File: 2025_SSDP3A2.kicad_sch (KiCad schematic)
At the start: 58 parts, among them J1 SolderPad, J2 SolderPad, J3 SolderPad, J4 SolderPad, J5 SolderPad_01x05, Q1 IAUZ30N10S5L240, Q2 BSZ096N10LS5, U1 LM5146RGYR

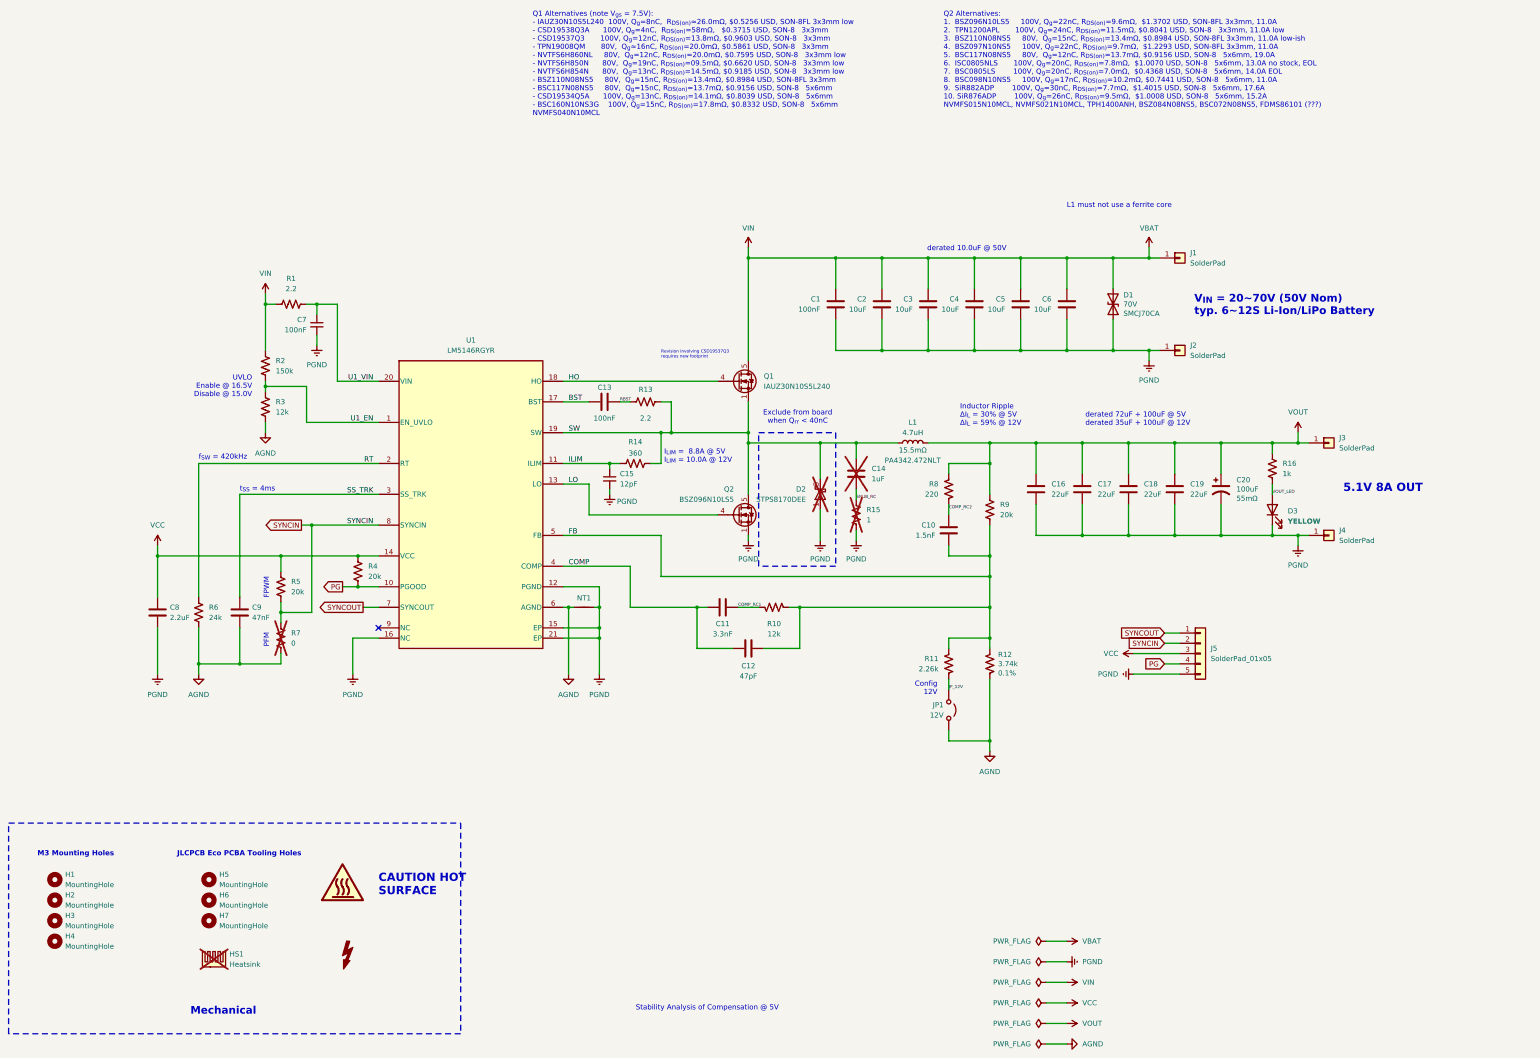
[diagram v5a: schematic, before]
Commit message: Added 7.4V output support
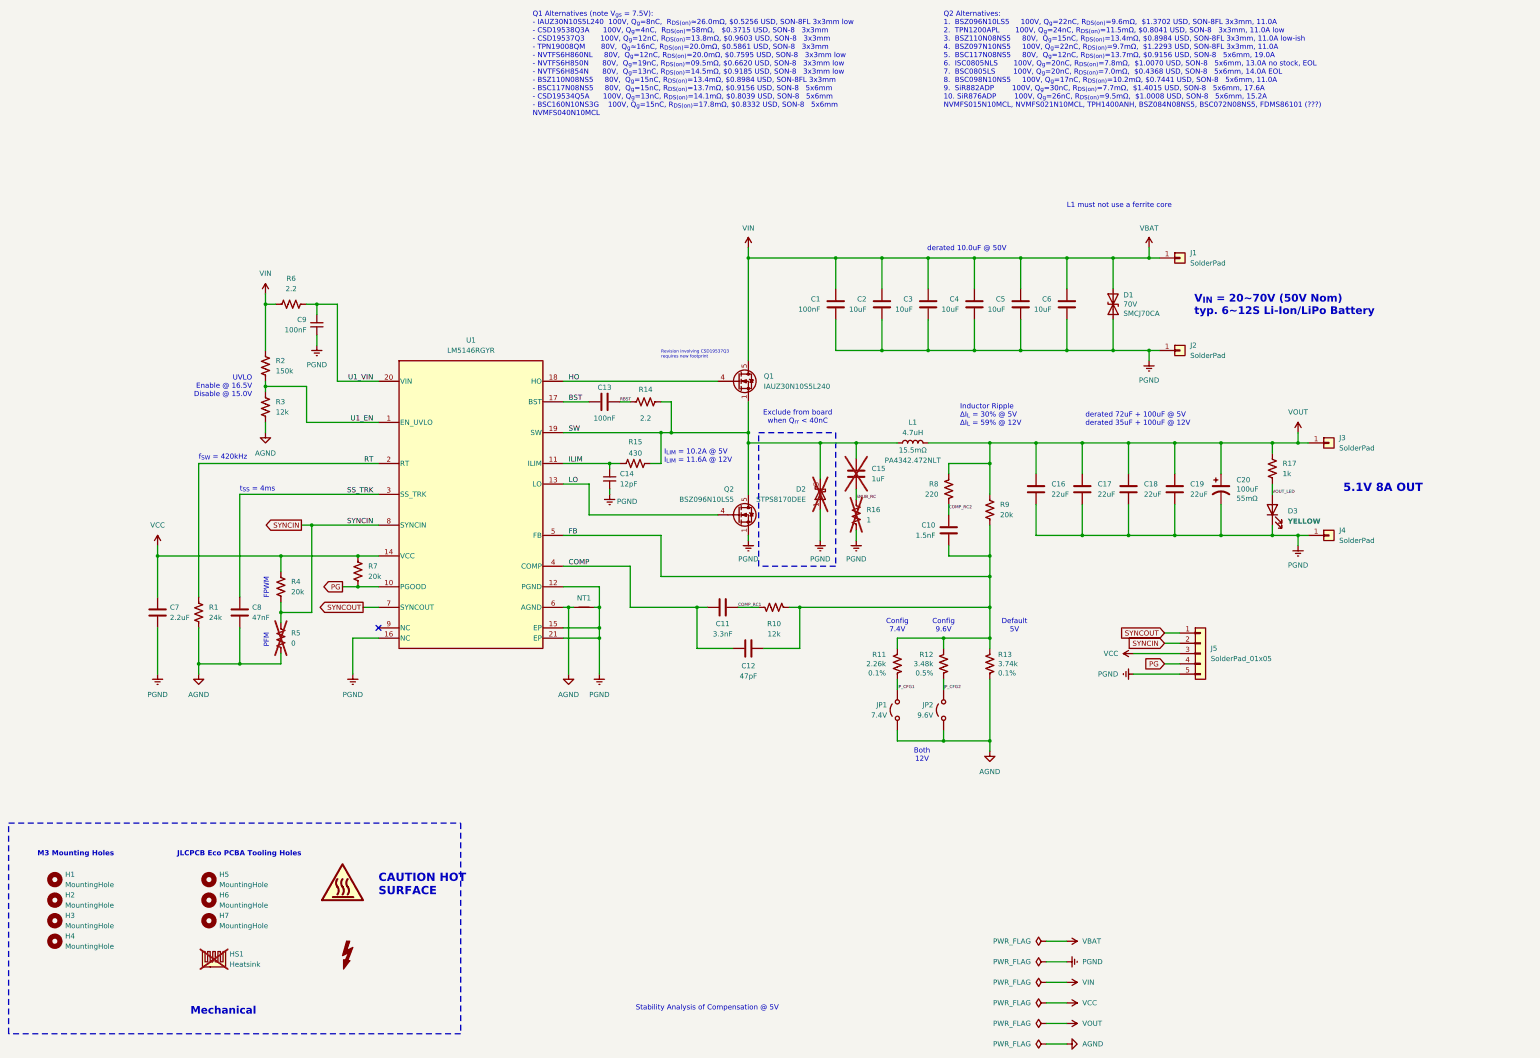
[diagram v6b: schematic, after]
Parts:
- added JP2: 9.6V, Jumper:SolderJumper-2_P1.3mm_Open_TrianglePad1.0x1.5mm, symbol Jumper:Jumper_2_Open
- added R12: 3.48k, Resistor_SMD:R_0603_1608Metric, symbol Device:R_US
- JP1: value 12V -> 7.4V
- R11: LCSC PN C667565 -> C861538; MANUFACTURER Guangdong Fenghua -> YAGEO; Tolerance 1% -> 0.1%
- R15: renamed from R14; value 360 -> 430; LCSC PN C25194 -> C23170
- renumbered C15 to C14, C14 to C15, C8 to C7, C9 to C8, C7 to C9, R6 to R1, R12 to R13, R13 to R14, R15 to R16, R16 to R17, R5 to R4, R7 to R5, R1 to R6, R4 to R7
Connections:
- net AGND: now also JP2.1 (A)
- net FB: now also R12.1
- net JP_12V renamed JP_CFG1
- new net JP_CFG2: JP2.2 (B), R12.2
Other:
- note added: "Both 12V"
- note added: "Config 7.4V"
- note added: "Config 9.6V"
- note added: "Default 5V"
- note added: "I_{LIM} = 10.2A @ 5V I_{LIM} = 11.6A @ 12V"
- note removed: "Config 12V"
- note removed: "I_{LIM} = 8.8A @ 5V I_{LIM} = 10.0A @ 12V"
- moved on the sheet: JP1, R11

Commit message: Final tweaks
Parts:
- HS1: value Heatsink -> 567-45AB
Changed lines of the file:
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@@
 			)
 		)
-		(property "Value" "Heatsink"
+		(property "Value" "567-45AB"
 			(at 77.47 260.985 0)
 			(effects

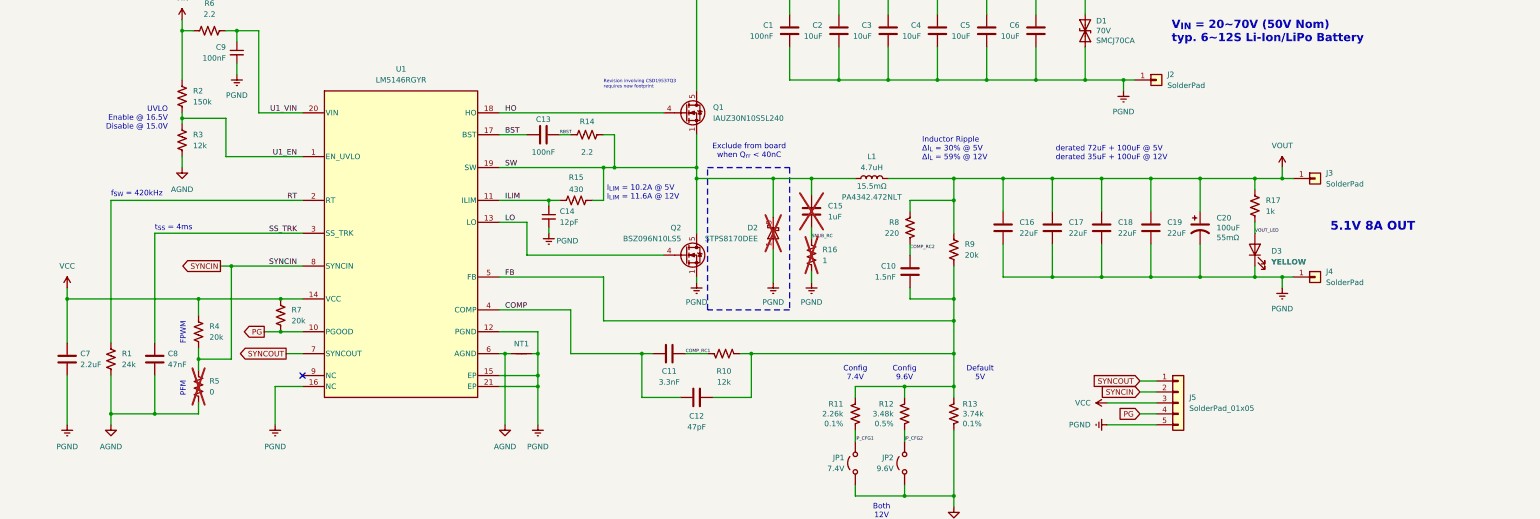
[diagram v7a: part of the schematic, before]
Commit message: Added more capacitors to meet overshoot requirements
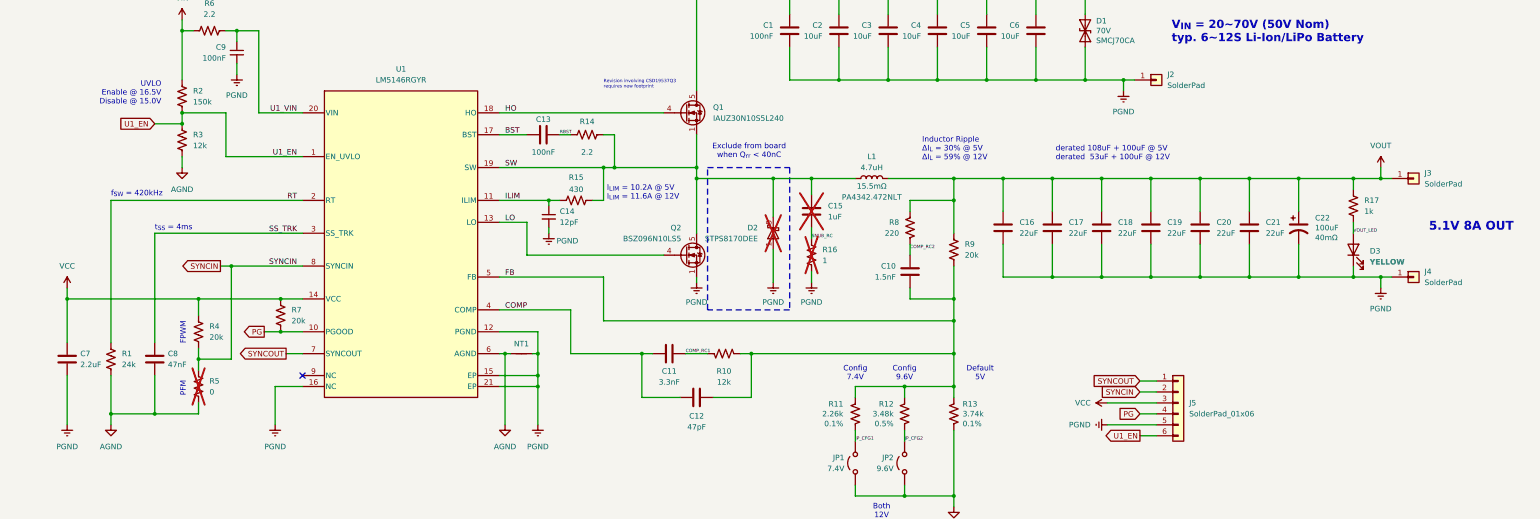
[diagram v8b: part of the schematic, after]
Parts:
- added C20, C21: 22uF, Capacitor_SMD:C_1210_3225Metric, symbol Device:C
- C22: renamed from C20; footprint Capacitor_Tantalum_SMD:CP_EIA-7343-30_AVX-N_HandSolder -> Capacitor_Tantalum_SMD:CP_EIA-7343-20_Kemet-V_HandSolder; ESR 55mΩ -> 40mΩ; MANUFACTURER Panasonic -> KEMET; Voltage 20V -> 25V
- J5: value SolderPad_01x05 -> SolderPad_01x06; footprint Connector_Custom:SolderWirePad_1x05_SMD_1.5x2mm -> Connector_Custom:SolderWirePad_1x06_SMD_1.5x2mm; symbol Connector_Generic:Conn_01x05 -> Connector_Generic:Conn_01x06
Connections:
- net PGND: now also C20.2, C21.2
- net U1_EN: now also J5.6 (Pin_6)
- net VOUT: now also C20.1, C21.1
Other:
- note added: "derated 108uF + 100uF @ 5V derated 53uF + 100uF @ 12V"
- note removed: "derated 72uF + 100uF @ 5V derated 35uF + 100uF @ 12V"
- moved on the sheet: C22, D3, J3, J4, R17
